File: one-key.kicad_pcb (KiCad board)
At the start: 2 copper layers, 3 parts, among them SW1 SW_SPST

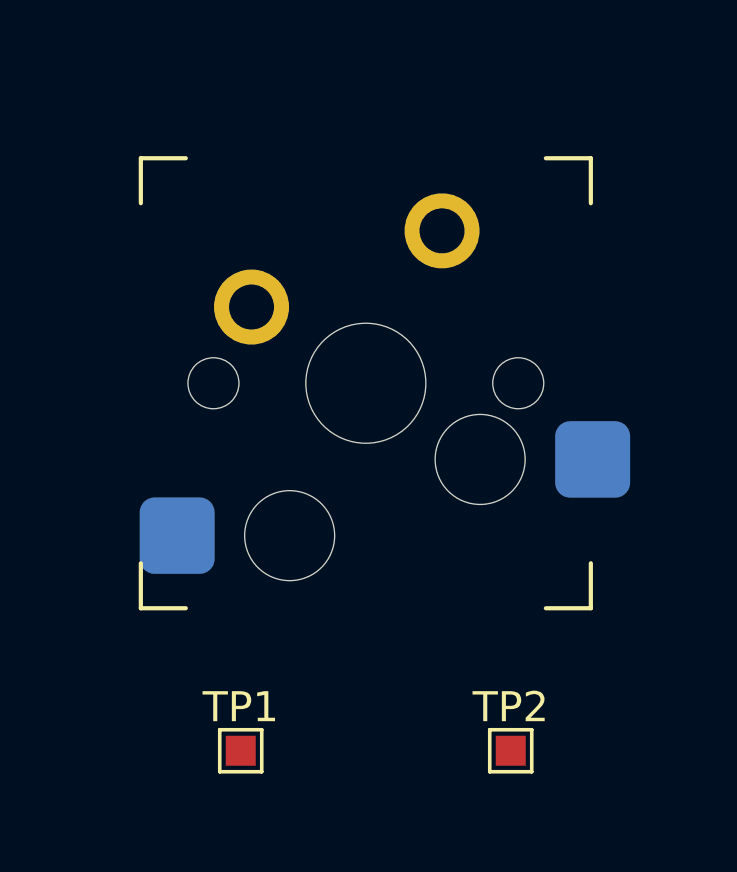
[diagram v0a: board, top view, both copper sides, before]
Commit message: 
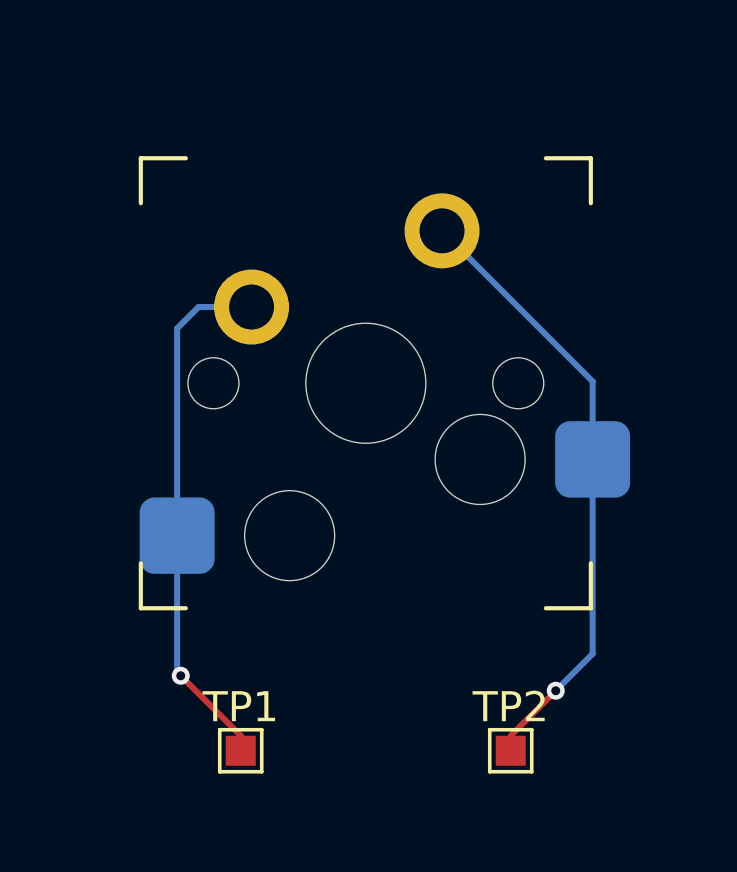
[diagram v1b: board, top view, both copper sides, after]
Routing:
- net Net-(SW1-B): track 0.00 -> 20.5 mm, vias 0 -> 1
- net Net-(SW1-A): track 0.00 -> 17.7 mm, vias 0 -> 1
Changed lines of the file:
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@@
 		)
 	)
+	(segment
+		(start 139 100.5)
+		(end 139 101)
+		(width 0.2)
+		(layer "F.Cu")
+		(net 1)
+	)
+	(segment
+		(start 137 98.5)
+		(end 139 100.5)
+		(width 0.2)
+		(layer "F.Cu")
+		(net 1)
+	)
+	(via
+		(at 137 98.5)
+		(size 0.6)
+		(drill 0.3)
+		(layers "F.Cu" "B.Cu")
+		(net 1)
+	)
+	(segment
+		(start 136.88 93.83)
+		(end 136.88 86.922234)
+		(width 0.2)
+		(layer "B.Cu")
+		(net 1)
+	)
+	(segment
+		(start 136.88 93.83)
+		(end 136.88 98.38)
+		(width 0.2)
+		(layer "B.Cu")
+		(net 1)
+	)
+	(segment
+		(start 136.88 86.922234)
+		(end 137.592234 86.21)
+		(width 0.2)
+		(layer "B.Cu")
+		(net 1)
+	)
+	(segment
+		(start 136.88 98.38)
+		(end 137 98.5)
+		(width 0.2)
+		(layer "B.Cu")
+		(net 1)
+	)
+	(segment
+		(start 137.592234 86.21)
+		(end 139.36 86.21)
+		(width 0.2)
+		(layer "B.Cu")
+		(net 1)
+	)
+	(segment
+		(start 148 100.5)
+		(end 148 101)
+		(width 0.2)
+		(layer "F.Cu")
+		(net 2)
+	)
+	(segment
+		(start 149.5 99)
+		(end 148 100.5)
+		(width 0.2)
+		(layer "F.Cu")
+		(net 2)
+	)
+	(via
+		(at 149.5 99)
+		(size 0.6)
+		(drill 0.3)
+		(layers "F.Cu" "B.Cu")
+		(net 2)
+	)
+	(segment
+		(start 150.73 91.29)
+		(end 150.73 88.69)
+		(width 0.2)
+		(layer "B.Cu")
+		(net 2)
+	)
+	(segment
+		(start 150.73 88.69)
+		(end 145.71 83.67)
+		(width 0.2)
+		(layer "B.Cu")
+		(net 2)
+	)
+	(segment
+		(start 150.73 97.77)
+		(end 149.5 99)
+		(width 0.2)
+		(layer "B.Cu")
+		(net 2)
+	)
+	(segment
+		(start 150.73 91.29)
+		(end 150.73 97.77)
+		(width 0.2)
+		(layer "B.Cu")
+		(net 2)
+	)
 )

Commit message: 
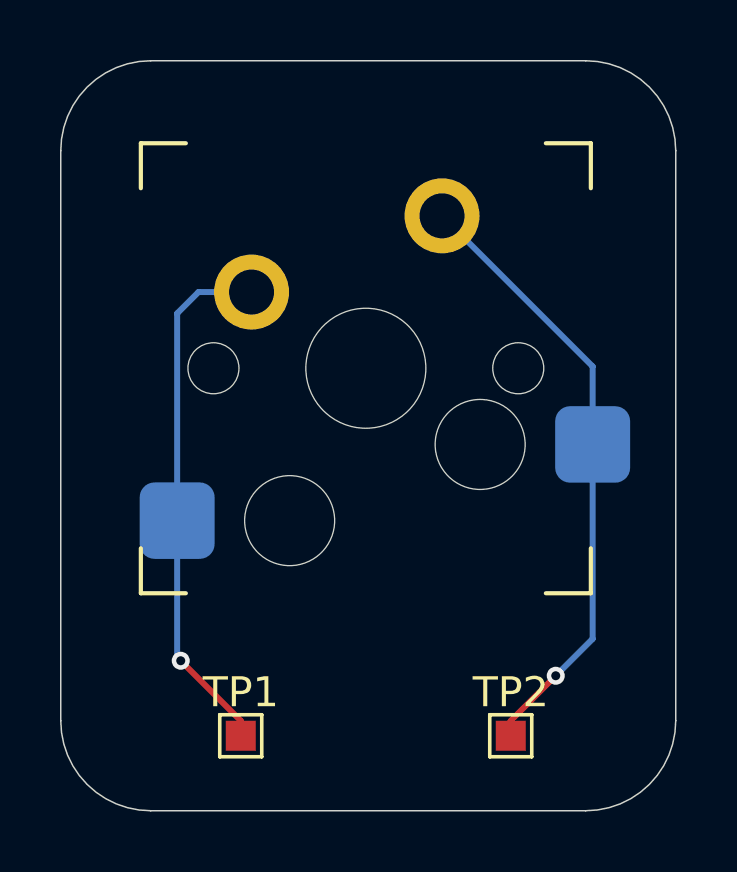
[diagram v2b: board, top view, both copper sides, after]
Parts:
- moved SW1 0.50 mm to (143.2, 88.2)
- moved TP1 0.50 mm to (139.0, 100.5)
- moved TP2 0.50 mm to (148.0, 100.5)
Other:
- board outline added: 20.5 x 25 mm
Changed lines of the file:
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@@
 	(footprint "key-switches:SW_MX_HotSwap_THT"
 		(layer "F.Cu")
-		(at 143.17 88.75)
+		(at 143.17 88.25)
 		(descr "Cherry MX style mechanical keyboard switch, Kailh/Gateron hot-swap socket and through-hole soldering, single-sided mounting.")
 		(tags "switch, hot_swap")
@@
 	(footprint "TestPoint:TestPoint_Pad_1.0x1.0mm"
 		(layer "F.Cu")
-		(at 139 101)
+		(at 139 100.5)
 		(descr "SMD rectangular pad as test Point, square 1.0mm side length")
 		(tags "test point SMD pad rectangle square")
@@
 	(footprint "TestPoint:TestPoint_Pad_1.0x1.0mm"
 		(layer "F.Cu")
-		(at 148 101)
+		(at 148 100.5)
 		(descr "SMD rectangular pad as test Point, square 1.0mm side length")
 		(tags "test point SMD pad rectangle square")
@@
 		)
 	)
-	(segment
-		(start 139 100.5)
-		(end 139 101)
+	(gr_arc
+		(start 133 81)
+		(mid 133.87868 78.87868)
+		(end 136 78)
+		(stroke
+			(width 0.05)
+			(type default)
+		)
+		(layer "Edge.Cuts")
+	)
+	(gr_line
+		(start 136 78)
+		(end 150.5 78)
+		(stroke
+			(width 0.05)
+			(type default)
+		)
+		(layer "Edge.Cuts")
+	)
+	(gr_line
+		(start 153.5 81)
+		(end 153.5 100)
+		(stroke
+			(width 0.05)
+			(type default)
+		)
+		(layer "Edge.Cuts")
+	)
+	(gr_arc
+		(start 136 103)
+		(mid 133.87868 102.12132)
+		(end 133 100)
+		(stroke
+			(width 0.05)
+			(type default)
+		)
+		(layer "Edge.Cuts")
+	)
+	(gr_arc
+		(start 153.5 100)
+		(mid 152.62132 102.12132)
+		(end 150.5 103)
+		(stroke
+			(width 0.05)
+			(type default)
+		)
+		(layer "Edge.Cuts")
+	)
+	(gr_line
+		(start 133 81)
+		(end 133 100)
+		(stroke
+			(width 0.05)
+			(type default)
+		)
+		(layer "Edge.Cuts")
+	)
+	(gr_arc
+		(start 150.5 78)
+		(mid 152.62132 78.87868)
+		(end 153.5 81)
+		(stroke
+			(width 0.05)
+			(type default)
+		)
+		(layer "Edge.Cuts")
+	)
+	(gr_line
+		(start 136 103)
+		(end 150.5 103)
+		(stroke
+			(width 0.05)
+			(type default)
+		)
+		(layer "Edge.Cuts")
+	)
+	(segment
+		(start 139 100)
+		(end 139 100.5)
 		(width 0.2)
 		(layer "F.Cu")
@@
 	)
 	(segment
-		(start 137 98.5)
-		(end 139 100.5)
+		(start 137 98)
+		(end 139 100)
 		(width 0.2)
 		(layer "F.Cu")
@@
 	)
 	(via
-		(at 137 98.5)
+		(at 137 98)
 		(size 0.6)
 		(drill 0.3)
@@
 	)
 	(segment
-		(start 136.88 93.83)
-		(end 136.88 86.922234)
+		(start 136.88 93.33)
+		(end 136.88 86.422234)
 		(width 0.2)
 		(layer "B.Cu")
@@
 	)
 	(segment
-		(start 136.88 93.83)
-		(end 136.88 98.38)
+		(start 136.88 93.33)
+		(end 136.88 97.88)
 		(width 0.2)
 		(layer "B.Cu")
@@
 	)
 	(segment
-		(start 136.88 86.922234)
-		(end 137.592234 86.21)
+		(start 136.88 86.422234)
+		(end 137.592234 85.71)
 		(width 0.2)
 		(layer "B.Cu")
@@
 	)
 	(segment
-		(start 136.88 98.38)
-		(end 137 98.5)
+		(start 136.88 97.88)
+		(end 137 98)
 		(width 0.2)
 		(layer "B.Cu")
@@
 	)
 	(segment
-		(start 137.592234 86.21)
-		(end 139.36 86.21)
+		(start 137.592234 85.71)
+		(end 139.36 85.71)
 		(width 0.2)
 		(layer "B.Cu")
@@
 	)
 	(segment
-		(start 148 100.5)
-		(end 148 101)
+		(start 148 100)
+		(end 148 100.5)
 		(width 0.2)
 		(layer "F.Cu")
@@
 	)
 	(segment
-		(start 149.5 99)
-		(end 148 100.5)
+		(start 149.5 98.5)
+		(end 148 100)
 		(width 0.2)
 		(layer "F.Cu")
@@
 	)
 	(via
-		(at 149.5 99)
+		(at 149.5 98.5)
 		(size 0.6)
 		(drill 0.3)
@@
 	)
 	(segment
-		(start 150.73 91.29)
-		(end 150.73 88.69)
+		(start 150.73 90.79)
+		(end 150.73 88.19)
 		(width 0.2)
 		(layer "B.Cu")
@@
 	)
 	(segment
-		(start 150.73 88.69)
-		(end 145.71 83.67)
+		(start 150.73 88.19)
+		(end 145.71 83.17)
 		(width 0.2)
 		(layer "B.Cu")
@@
 	)
 	(segment
-		(start 150.73 97.77)
-		(end 149.5 99)
+		(start 150.73 97.27)
+		(end 149.5 98.5)
 		(width 0.2)
 		(layer "B.Cu")
@@
 	)
 	(segment
-		(start 150.73 91.29)
-		(end 150.73 97.77)
+		(start 150.73 90.79)
+		(end 150.73 97.27)
 		(width 0.2)
 		(layer "B.Cu")
